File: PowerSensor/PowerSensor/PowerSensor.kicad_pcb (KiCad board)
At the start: 2 copper layers, 35.6 x 22.6 mm, 12 parts, among them J1 Current Sens, J3 BAT+, J4 BAT-, J5 Screw_Terminal_01x04, U1 ACS712ELCTR-20A-T_NRND

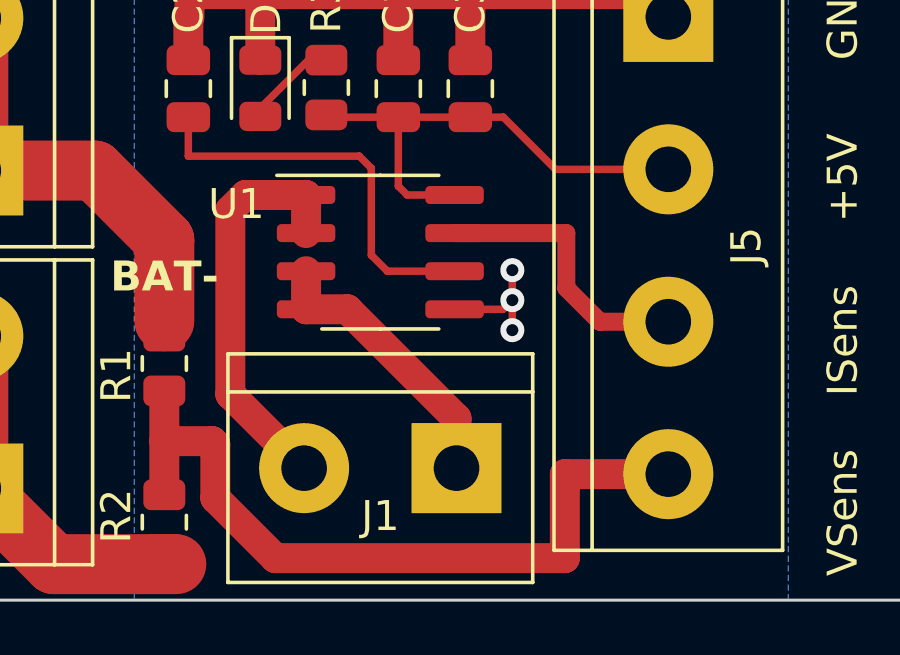
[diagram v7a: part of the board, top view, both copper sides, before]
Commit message: Change the filter Cap value 1nF
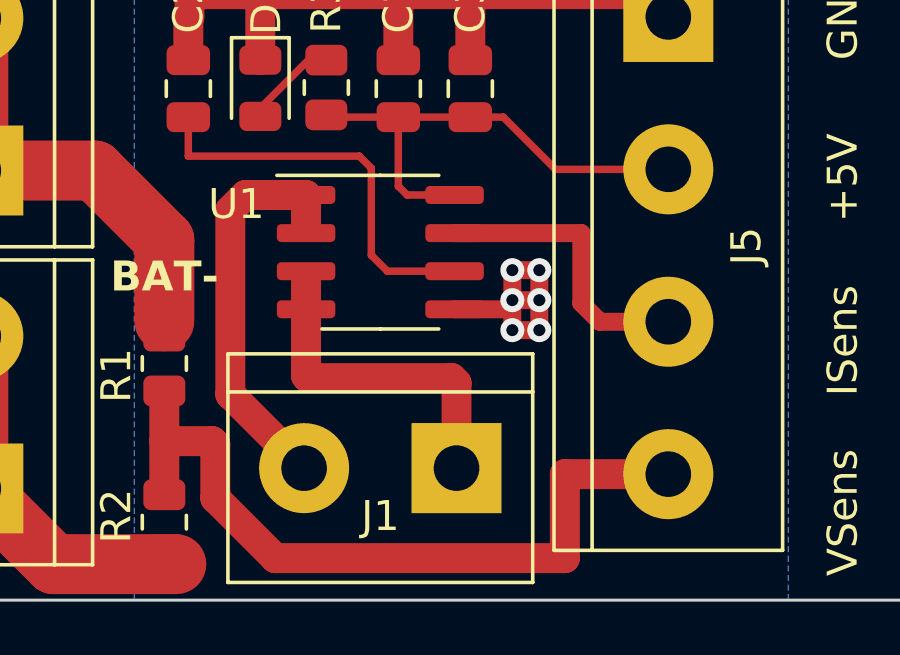
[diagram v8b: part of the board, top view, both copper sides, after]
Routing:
- net GND: track 29.1 -> 33.8 mm, vias 3 -> 6
- net IN-: track 9.45 -> 11.2 mm
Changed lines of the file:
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@@
     (effects (font (size 1 1) (thickness 0.15)) (justify left bottom))
   )
+  (segment (start 114.5 94.8) (end 114.5 92.8) (width 0.6) (layer "F.Cu") (net 1))
   (segment (start 102.9 83.575) (end 102.84 83.635) (width 1) (layer "F.Cu") (net 1))
-  (segment (start 111.675 94.105) (end 113.295 94.105) (width 0.25) (layer "F.Cu") (net 1))
+  (segment (start 111.675 94.105) (end 113.295 94.105) (width 0.6) (layer "F.Cu") (net 1))
+  (segment (start 113.6 94.8) (end 114.5 94.8) (width 0.6) (layer "F.Cu") (net 1))
   (segment (start 105.2 85.8) (end 105.2 83.6) (width 1) (layer "F.Cu") (net 1))
   (segment (start 113.295 94.105) (end 113.6 93.8) (width 0.25) (layer "F.Cu") (net 1))
   (segment (start 118.8 84.36) (end 118.04 83.6) (width 1) (layer "F.Cu") (net 1))
   (segment (start 102.84 84.36) (end 102.8 84.4) (width 0.25) (layer "F.Cu") (net 1))
+  (segment (start 113.6 93.8) (end 114.5 93.8) (width 0.6) (layer "F.Cu") (net 1))
+  (segment (start 114.5 92.8) (end 113.6 92.8) (width 0.6) (layer "F.Cu") (net 1))
   (segment (start 112.2 85.8) (end 112.2 83.6) (width 1) (layer "F.Cu") (net 1))
   (segment (start 102.925 83.6) (end 102.9 83.575) (width 1) (layer "F.Cu") (net 1))
   (segment (start 102.8 84.4) (end 102.8 85.8) (width 1) (layer "F.Cu") (net 1))
-  (segment (start 113.6 92.8) (end 113.6 94.8) (width 0.25) (layer "F.Cu") (net 1))
   (segment (start 118.04 83.6) (end 102.925 83.6) (width 1) (layer "F.Cu") (net 1))
+  (segment (start 113.6 92.8) (end 113.6 94.8) (width 0.6) (layer "F.Cu") (net 1))
   (segment (start 109.8 85.8) (end 109.8 83.6) (width 1) (layer "F.Cu") (net 1))
   (segment (start 102.84 83.635) (end 102.84 84.36) (width 1) (layer "F.Cu") (net 1))
   (via (at 113.6 93.8) (size 0.8) (drill 0.4) (layers "F.Cu" "B.Cu") (free) (net 1))
+  (via (at 114.5 93.8) (size 0.8) (drill 0.4) (layers "F.Cu" "B.Cu") (free) (net 1))
   (via (at 113.6 94.8) (size 0.8) (drill 0.4) (layers "F.Cu" "B.Cu") (free) (net 1))
+  (via (at 114.5 94.8) (size 0.8) (drill 0.4) (layers "F.Cu" "B.Cu") (free) (net 1))
+  (via (at 114.5 92.8) (size 0.8) (drill 0.4) (layers "F.Cu" "B.Cu") (free) (net 1))
   (via (at 113.6 92.8) (size 0.8) (drill 0.4) (layers "F.Cu" "B.Cu") (free) (net 1))
   (segment (start 107.4 85.8) (end 106.8 85.8) (width 0.25) (layer "F.Cu") (net 2))
   (segment (start 105.2 87.4) (end 105.2 87.675) (width 0.25) (layer "F.Cu") (net 2))
   (segment (start 106.8 85.8) (end 105.2 87.4) (width 0.25) (layer "F.Cu") (net 2))
-  (segment (start 111.74 99.12) (end 111.74 97.74) (width 1) (layer "F.Cu") (net 3))
-  (segment (start 108.105 94.105) (end 106.725 94.105) (width 1) (layer "F.Cu") (net 3))
-  (segment (start 111.74 97.74) (end 108.105 94.105) (width 1) (layer "F.Cu") (net 3))
+  (segment (start 111.74 99.12) (end 111.74 96.56) (width 1) (layer "F.Cu") (net 3))
   (segment (start 111.74 99.4) (end 111.74 99.12) (width 0.2) (layer "F.Cu") (net 3))
-  (segment (start 106.725 94.105) (end 106.725 92.835) (width 1) (layer "F.Cu") (net 3))
+  (segment (start 111.74 96.56) (end 111.58 96.4) (width 1) (layer "F.Cu") (net 3))
+  (segment (start 106.725 96.325) (end 106.725 94.105) (width 1) (layer "F.Cu") (net 3))
+  (segment (start 106.725 94.105) (end 106.725 93.1) (width 1) (layer "F.Cu") (net 3))
+  (segment (start 106.8 96.4) (end 106.725 96.325) (width 1) (layer "F.Cu") (net 3))
+  (segment (start 111.58 96.4) (end 106.8 96.4) (width 1) (layer "F.Cu") (net 3))
   (segment (start 106.66 99.4) (end 104.2 96.94) (width 1) (layer "F.Cu") (net 4))
   (segment (start 104.705 90.295) (end 106.725 90.295) (width 1) (layer "F.Cu") (net 4))
   (segment (start 104.2 90.8) (end 104.705 90.295) (width 1) (layer "F.Cu") (net 4))
   (segment (start 104.2 96.94) (end 104.2 90.8) (width 1) (layer "F.Cu") (net 4))
-  (segment (start 106.725 90.295) (end 106.725 91.565) (width 1) (layer "F.Cu") (net 4))
+  (segment (start 106.725 90.295) (end 106.725 91.3) (width 1) (layer "F.Cu") (net 4))
   (segment (start 102.4 102.6) (end 98.32 102.6) (width 2) (layer "F.Cu") (net 5))
   (segment (start 95.8 95) (end 95.8 100.08) (width 2) (layer "F.Cu") (net 5))
@@
   (segment (start 112.2 87.7) (end 109.8 87.7) (width 0.25) (layer "F.Cu") (net 6))
   (segment (start 109.8 87.7) (end 109.8 90) (width 0.25) (layer "F.Cu") (net 6))
-  (segment (start 115.4 91.565) (end 115.4 93.4) (width 0.6) (layer "F.Cu") (net 7))
+  (segment (start 115.9 91.565) (end 115.9 93.9) (width 0.6) (layer "F.Cu") (net 7))
+  (segment (start 115.9 93.9) (end 116.52 94.52) (width 0.6) (layer "F.Cu") (net 7))
+  (segment (start 111.675 91.565) (end 115.9 91.565) (width 0.6) (layer "F.Cu") (net 7))
   (segment (start 116.52 94.52) (end 118.8 94.52) (width 0.6) (layer "F.Cu") (net 7))
-  (segment (start 111.675 91.565) (end 115.4 91.565) (width 0.6) (layer "F.Cu") (net 7))
-  (segment (start 115.4 93.4) (end 116.52 94.52) (width 0.6) (layer "F.Cu") (net 7))
   (segment (start 115.35 99.6) (end 118.8 99.6) (width 1) (layer "F.Cu") (net 8))
   (segment (start 105.7 102.4) (end 115.35 102.4) (width 1) (layer "F.Cu") (net 8))
